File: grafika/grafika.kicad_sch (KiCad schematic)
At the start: 6 parts, among them Q1 2N7000, U1 ESP32-C3-WROOM-02

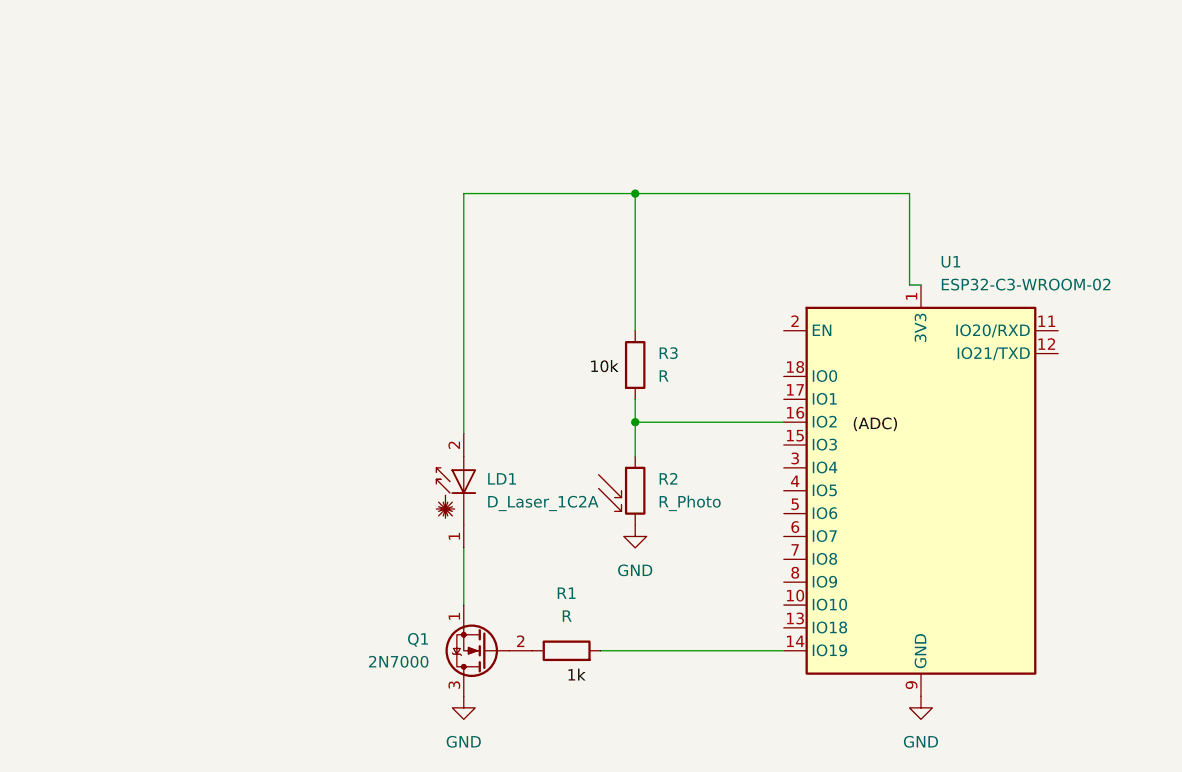
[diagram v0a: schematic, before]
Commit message: Added new Schematics and updated README.md accordingly. Chaged KiCad to be more precise.
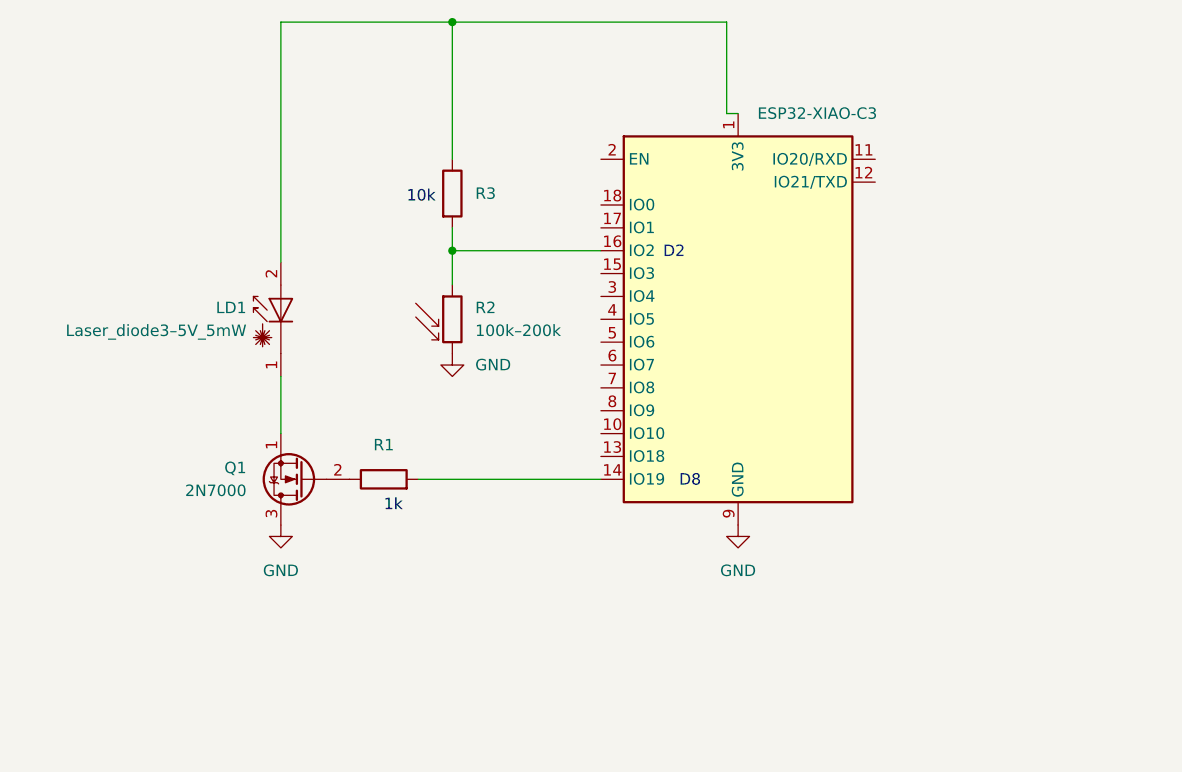
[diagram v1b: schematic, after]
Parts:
- LD1: value D_Laser_1C2A -> Laser_diode3–5V_5mW
- R2: value R_Photo -> 100k–200k
- R3: value R -> ~
- U1: value ESP32-C3-WROOM-02 -> ESP32-XIAO-C3
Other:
- note added: "D2"
- note added: "D8"
- title: (none) -> Laser detector for accelerator model
- moved on the sheet: LD1, Q1, R1, R2, R3
